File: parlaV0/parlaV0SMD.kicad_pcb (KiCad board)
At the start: 2 copper layers, 13 parts, among them U1 LM386

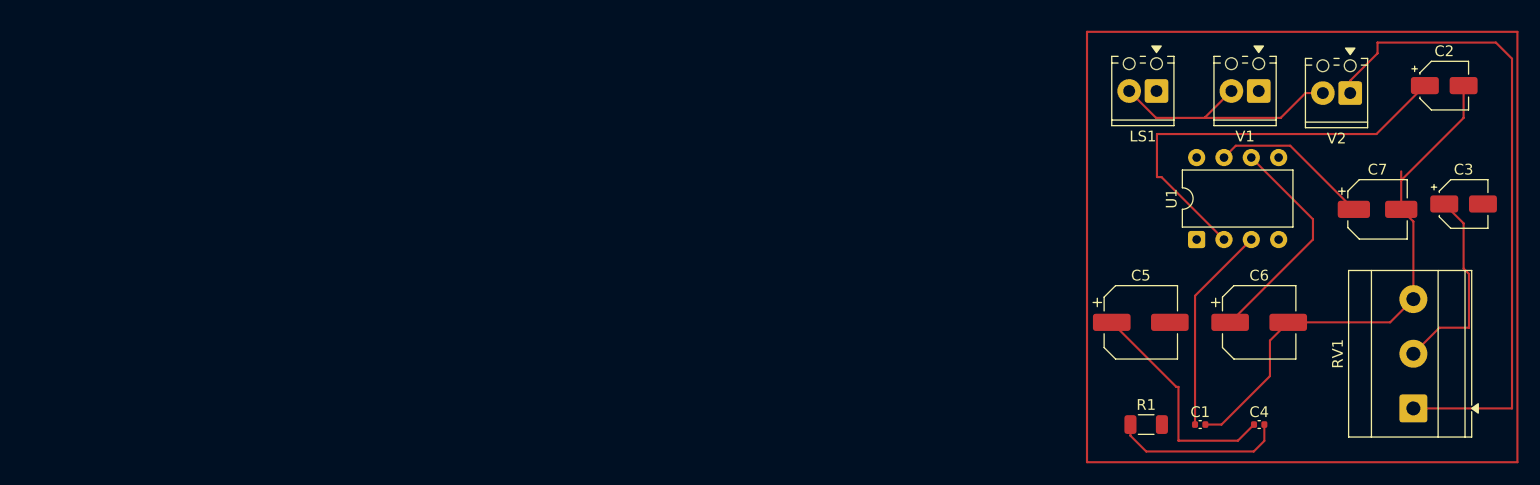
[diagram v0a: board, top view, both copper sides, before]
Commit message: agregar nuevo ruteo
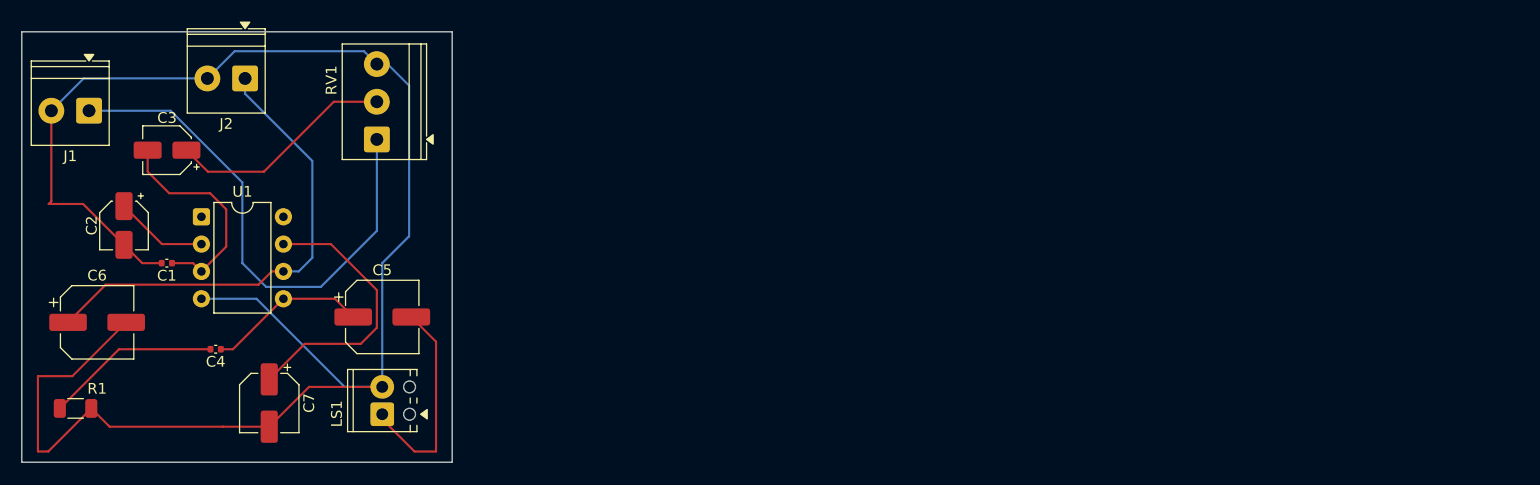
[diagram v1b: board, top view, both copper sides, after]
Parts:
- removed V1: 6, TerminalBlock_Phoenix:TerminalBlock_Phoenix_MPT-0,5-2-2.54_1x02_P2.54mm_Horizontal
- removed V2: 1, TerminalBlock_Phoenix:TerminalBlock_Phoenix_MPT-0,5-2-2.54_1x02_P2.54mm_Horizontal
- added J1: Screw_Terminal_01x02, TerminalBlock_Phoenix:TerminalBlock_Phoenix_PT-1,5-2-3.5-H_1x02_P3.50mm_Horizontal, F.Cu at (106.8, 57.3)
- added J2: Screw_Terminal_01x02, TerminalBlock_Phoenix:TerminalBlock_Phoenix_PT-1,5-2-3.5-H_1x02_P3.50mm_Horizontal, F.Cu at (121.2, 54.3)
- R1: value 10 -> 10R
- RV1: footprint TerminalBlock_Phoenix:TerminalBlock_Phoenix_MKDS-3-3-5.08_1x03_P5.08mm_Horizontal -> TerminalBlock_Phoenix:TerminalBlock_Phoenix_PT-1,5-3-3.5-H_1x03_P3.50mm_Horizontal
- moved C2 123.4 mm to (110.0, 68.0), turned to -90 degrees
- moved C3 120.6 mm to (114.0, 61.0), turned to 180 degrees
- moved C6 108.0 mm to (107.5, 77.0)
- moved C7 104.6 mm to (123.5, 84.5), turned to -90 degrees
- moved RV1 99.5 mm to (133.5, 60.0)
- moved R1 99.5 mm to (105.5, 85.0)
- moved C4 97.2 mm to (118.5, 79.5), turned to 180 degrees
- moved C1 97.2 mm to (114.0, 71.5), turned to 180 degrees
- moved U1 92.5 mm to (117.2, 67.2), turned to 0 degrees
- moved LS1 78.0 mm to (134.0, 85.5), turned to 90 degrees
- moved C5 70.5 mm to (134.0, 76.5)
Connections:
- net 0 renamed GND
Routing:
- net GND: track 73.1 -> 160.8 mm
- net Net-(U1--): track 39.4 -> 8.66 mm
- net +6V: track 20.9 -> 44.4 mm
- net Net-(C5-Pad2): track 0.00 -> 20.2 mm
- net /Vin: track 60.5 -> 48.6 mm
- net Net-(U1-BYPASS): track 15.0 -> 25.9 mm
- net Net-(C4-Pad1): track 21.3 -> 14.9 mm
- net Net-(C3-Pad1): track 18.6 -> 21.2 mm
- net Net-(U1-+): track 19.4 -> 20.5 mm
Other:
- board outline added: 40 x 40 mm

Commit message: agregar csv
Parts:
- moved J2 4.54 mm to (124.5, 57.5)
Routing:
- net GND: track 160.8 -> 165.4 mm
- net +6V: track 44.4 -> 39.9 mm
